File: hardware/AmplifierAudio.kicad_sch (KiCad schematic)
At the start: 50 parts, among them Q201 IRF9358, U201 MA12070P

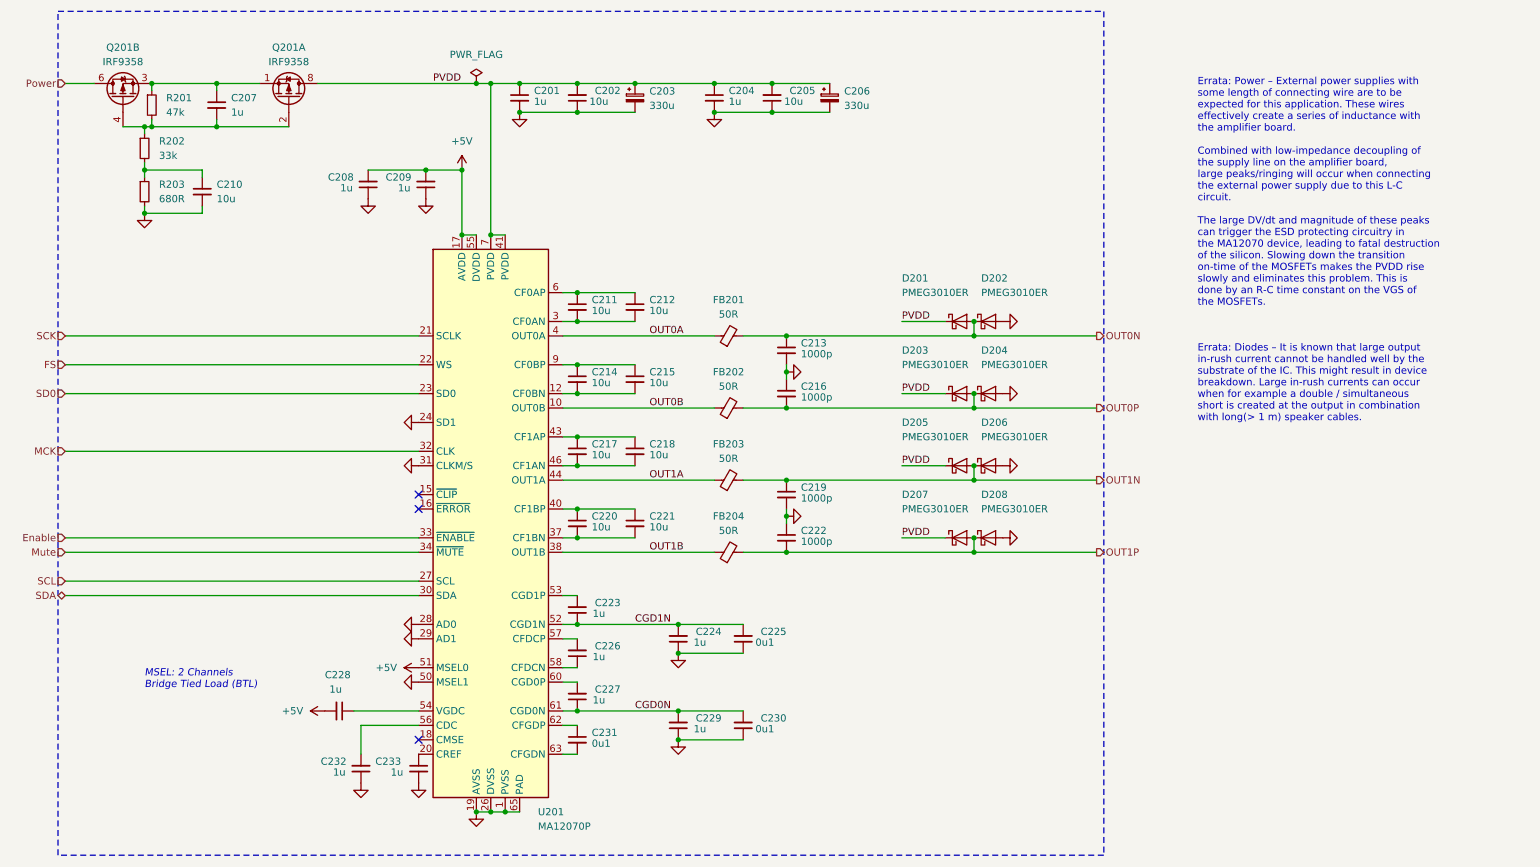
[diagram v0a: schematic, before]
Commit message: Replace Order_Number
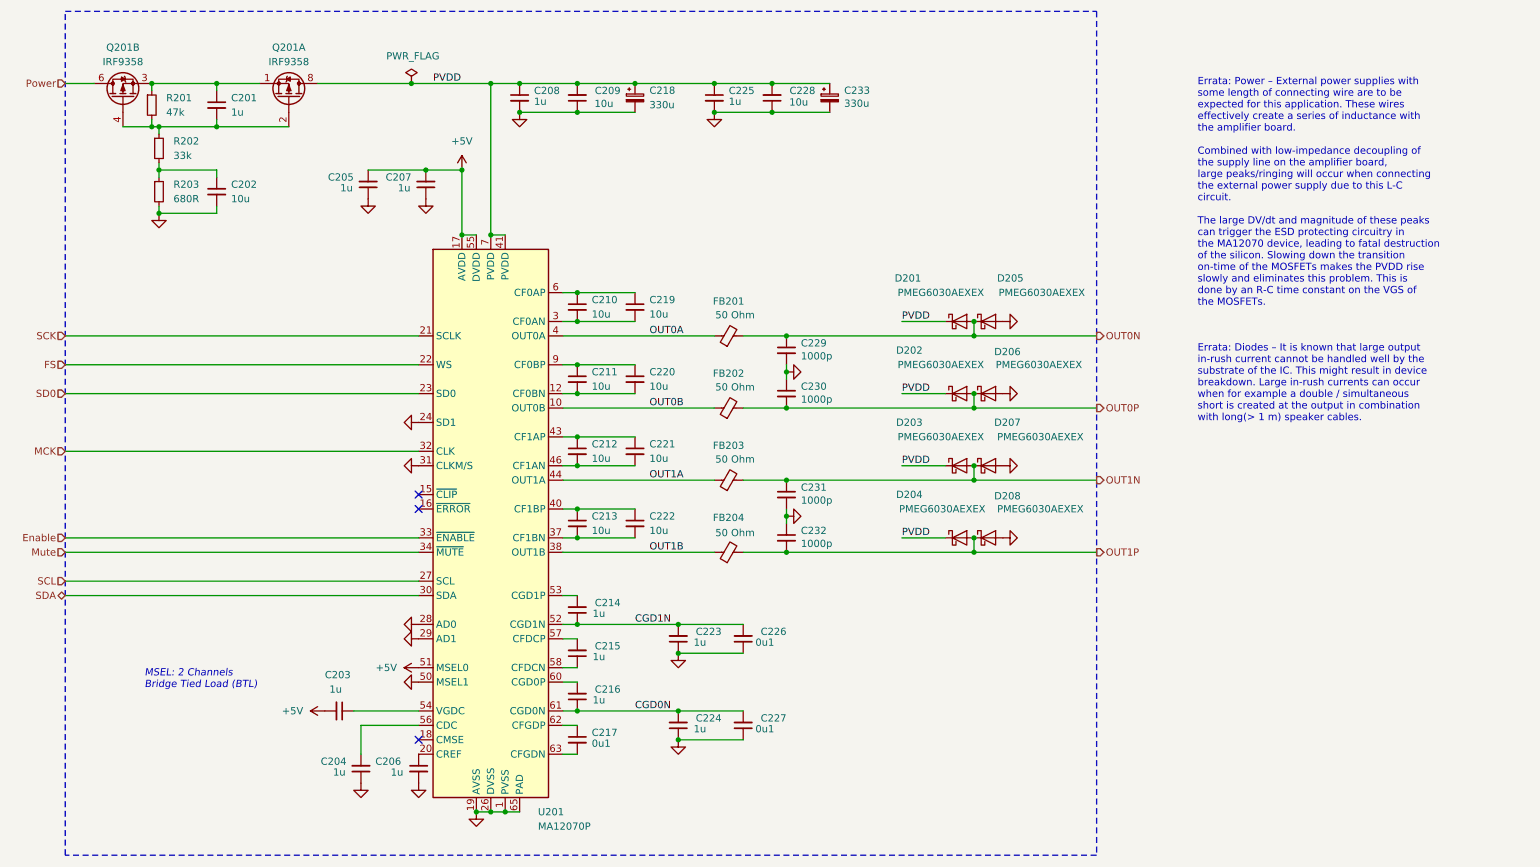
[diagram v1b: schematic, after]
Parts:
- C201: renamed from C207; footprint Capacitor_SMD:C_0603_1608Metric -> V2_Capacitor_SMD:C_0603; symbol Device:C_Small -> V2_Device:C_0603_1u; Manufacturer (none) -> TDK; Mouser (none) -> 810-CGA3E3X7R1H105K0; Product (none) -> CGA3E3X7R1H105K080AB; Rating (none) -> 50V
- C202: renamed from C210; footprint Capacitor_SMD:C_0805_2012Metric -> V2_Capacitor_SMD:C_0603; symbol Device:C_Small -> V2_Device:C_0603_10u; Manufacturer (none) -> TDK; Mouser (none) -> 810-C1608X6S1A106M; Product (none) -> C1608X6S1A106M080AC; Rating (none) -> 10V
- C203: renamed from C228; footprint Capacitor_SMD:C_0603_1608Metric -> V2_Capacitor_SMD:C_0603; symbol Device:C_Small -> V2_Device:C_0603_1u; Manufacturer (none) -> TDK; Mouser (none) -> 810-CGA3E3X7R1H105K0; Product (none) -> CGA3E3X7R1H105K080AB; Rating (none) -> 50V
- C204: renamed from C232; footprint Capacitor_SMD:C_0603_1608Metric -> V2_Capacitor_SMD:C_0603; symbol Device:C_Small -> V2_Device:C_0603_1u; Manufacturer (none) -> TDK; Mouser (none) -> 810-CGA3E3X7R1H105K0; Product (none) -> CGA3E3X7R1H105K080AB; Rating (none) -> 50V
- C205: renamed from C208; footprint Capacitor_SMD:C_0603_1608Metric -> V2_Capacitor_SMD:C_0603; symbol Device:C_Small -> V2_Device:C_0603_1u; Manufacturer (none) -> TDK; Mouser (none) -> 810-CGA3E3X7R1H105K0; Product (none) -> CGA3E3X7R1H105K080AB; Rating (none) -> 50V
- C206: renamed from C233; footprint Capacitor_SMD:C_0603_1608Metric -> V2_Capacitor_SMD:C_0603; symbol Device:C_Small -> V2_Device:C_0603_1u; Manufacturer (none) -> TDK; Mouser (none) -> 810-CGA3E3X7R1H105K0; Product (none) -> CGA3E3X7R1H105K080AB; Rating (none) -> 50V
- C207: renamed from C209; footprint Capacitor_SMD:C_0603_1608Metric -> V2_Capacitor_SMD:C_0603; symbol Device:C_Small -> V2_Device:C_0603_1u; Manufacturer (none) -> TDK; Mouser (none) -> 810-CGA3E3X7R1H105K0; Product (none) -> CGA3E3X7R1H105K080AB; Rating (none) -> 50V
- C208: renamed from C201; footprint Capacitor_SMD:C_0603_1608Metric -> V2_Capacitor_SMD:C_0603; symbol Device:C_Small -> V2_Device:C_0603_1u; Manufacturer (none) -> TDK; Mouser (none) -> 810-CGA3E3X7R1H105K0; Product (none) -> CGA3E3X7R1H105K080AB; Rating (none) -> 50V
- C209: renamed from C202; footprint Capacitor_SMD:C_0805_2012Metric -> V2_Capacitor_SMD:C_0603; symbol Device:C_Small -> V2_Device:C_0603_10u; Manufacturer (none) -> TDK; Mouser (none) -> 810-C1608X6S1A106M; Product (none) -> C1608X6S1A106M080AC; Rating (none) -> 10V
- C210: renamed from C211; footprint Capacitor_SMD:C_0805_2012Metric -> V2_Capacitor_SMD:C_0603; symbol Device:C_Small -> V2_Device:C_0603_10u; Manufacturer (none) -> TDK; Mouser (none) -> 810-C1608X6S1A106M; Product (none) -> C1608X6S1A106M080AC; Rating (none) -> 10V
- C211: renamed from C214; footprint Capacitor_SMD:C_0805_2012Metric -> V2_Capacitor_SMD:C_0603; symbol Device:C_Small -> V2_Device:C_0603_10u; Manufacturer (none) -> TDK; Mouser (none) -> 810-C1608X6S1A106M; Product (none) -> C1608X6S1A106M080AC; Rating (none) -> 10V
- C212: renamed from C217; footprint Capacitor_SMD:C_0805_2012Metric -> V2_Capacitor_SMD:C_0603; symbol Device:C_Small -> V2_Device:C_0603_10u; Manufacturer (none) -> TDK; Mouser (none) -> 810-C1608X6S1A106M; Product (none) -> C1608X6S1A106M080AC; Rating (none) -> 10V
- C213: renamed from C220; footprint Capacitor_SMD:C_0805_2012Metric -> V2_Capacitor_SMD:C_0603; symbol Device:C_Small -> V2_Device:C_0603_10u; Manufacturer (none) -> TDK; Mouser (none) -> 810-C1608X6S1A106M; Product (none) -> C1608X6S1A106M080AC; Rating (none) -> 10V
- C214: renamed from C223; footprint Capacitor_SMD:C_0603_1608Metric -> V2_Capacitor_SMD:C_0603; symbol Device:C_Small -> V2_Device:C_0603_1u; Manufacturer (none) -> TDK; Mouser (none) -> 810-CGA3E3X7R1H105K0; Product (none) -> CGA3E3X7R1H105K080AB; Rating (none) -> 50V
- C215: renamed from C226; footprint Capacitor_SMD:C_0603_1608Metric -> V2_Capacitor_SMD:C_0603; symbol Device:C_Small -> V2_Device:C_0603_1u; Manufacturer (none) -> TDK; Mouser (none) -> 810-CGA3E3X7R1H105K0; Product (none) -> CGA3E3X7R1H105K080AB; Rating (none) -> 50V
- C216: renamed from C227; footprint Capacitor_SMD:C_0603_1608Metric -> V2_Capacitor_SMD:C_0603; symbol Device:C_Small -> V2_Device:C_0603_1u; Manufacturer (none) -> TDK; Mouser (none) -> 810-CGA3E3X7R1H105K0; Product (none) -> CGA3E3X7R1H105K080AB; Rating (none) -> 50V
- C217: renamed from C231; footprint Capacitor_SMD:C_0603_1608Metric -> V2_Capacitor_SMD:C_0603; symbol Device:C_Small -> V2_Device:C_0603_0u1; Manufacturer (none) -> TDK; Mouser (none) -> 810-CGA3E2X7R1H104MA; Product (none) -> CGA3E2X7R1H104M080AA; Rating (none) -> 50V
- C218: renamed from C203; footprint Capacitor_SMD:CP_Elec_8x10 -> V2_Capacitor_SMD:CP_Elec_8x10; symbol Device:C_Polarized_Small -> V2_Device:C_Polarized_8x10.2_330u; Manufacturer (none) -> Panasonic; Mouser (none) -> 667-EEE-FT1V331GP; Product (none) -> EEE-FT1V331GP; Rating (none) -> 35V
- C219: renamed from C212; footprint Capacitor_SMD:C_0805_2012Metric -> V2_Capacitor_SMD:C_0603; symbol Device:C_Small -> V2_Device:C_0603_10u; Manufacturer (none) -> TDK; Mouser (none) -> 810-C1608X6S1A106M; Product (none) -> C1608X6S1A106M080AC; Rating (none) -> 10V
- C220: renamed from C215; footprint Capacitor_SMD:C_0805_2012Metric -> V2_Capacitor_SMD:C_0603; symbol Device:C_Small -> V2_Device:C_0603_10u; Manufacturer (none) -> TDK; Mouser (none) -> 810-C1608X6S1A106M; Product (none) -> C1608X6S1A106M080AC; Rating (none) -> 10V
- C221: renamed from C218; footprint Capacitor_SMD:C_0805_2012Metric -> V2_Capacitor_SMD:C_0603; symbol Device:C_Small -> V2_Device:C_0603_10u; Manufacturer (none) -> TDK; Mouser (none) -> 810-C1608X6S1A106M; Product (none) -> C1608X6S1A106M080AC; Rating (none) -> 10V
- C222: renamed from C221; footprint Capacitor_SMD:C_0805_2012Metric -> V2_Capacitor_SMD:C_0603; symbol Device:C_Small -> V2_Device:C_0603_10u; Manufacturer (none) -> TDK; Mouser (none) -> 810-C1608X6S1A106M; Product (none) -> C1608X6S1A106M080AC; Rating (none) -> 10V
- C223: renamed from C224; footprint Capacitor_SMD:C_0603_1608Metric -> V2_Capacitor_SMD:C_0603; symbol Device:C_Small -> V2_Device:C_0603_1u; Manufacturer (none) -> TDK; Mouser (none) -> 810-CGA3E3X7R1H105K0; Product (none) -> CGA3E3X7R1H105K080AB; Rating (none) -> 50V
- C224: renamed from C229; footprint Capacitor_SMD:C_0603_1608Metric -> V2_Capacitor_SMD:C_0603; symbol Device:C_Small -> V2_Device:C_0603_1u; Manufacturer (none) -> TDK; Mouser (none) -> 810-CGA3E3X7R1H105K0; Product (none) -> CGA3E3X7R1H105K080AB; Rating (none) -> 50V
- C225: renamed from C204; footprint Capacitor_SMD:C_0603_1608Metric -> V2_Capacitor_SMD:C_0603; symbol Device:C_Small -> V2_Device:C_0603_1u; Manufacturer (none) -> TDK; Mouser (none) -> 810-CGA3E3X7R1H105K0; Product (none) -> CGA3E3X7R1H105K080AB; Rating (none) -> 50V
- C226: renamed from C225; footprint Capacitor_SMD:C_0603_1608Metric -> V2_Capacitor_SMD:C_0603; symbol Device:C_Small -> V2_Device:C_0603_0u1; Manufacturer (none) -> TDK; Mouser (none) -> 810-CGA3E2X7R1H104MA; Product (none) -> CGA3E2X7R1H104M080AA; Rating (none) -> 50V
- C227: renamed from C230; footprint Capacitor_SMD:C_0603_1608Metric -> V2_Capacitor_SMD:C_0603; symbol Device:C_Small -> V2_Device:C_0603_0u1; Manufacturer (none) -> TDK; Mouser (none) -> 810-CGA3E2X7R1H104MA; Product (none) -> CGA3E2X7R1H104M080AA; Rating (none) -> 50V
- C228: renamed from C205; footprint Capacitor_SMD:C_0805_2012Metric -> V2_Capacitor_SMD:C_0603; symbol Device:C_Small -> V2_Device:C_0603_10u; Manufacturer (none) -> TDK; Mouser (none) -> 810-C1608X6S1A106M; Product (none) -> C1608X6S1A106M080AC; Rating (none) -> 10V
- C229: renamed from C213; footprint Capacitor_SMD:C_0603_1608Metric -> V2_Capacitor_SMD:C_0603; symbol Device:C_Small -> V2_Device:C_0603_1000p; Manufacturer (none) -> TDK; Mouser (none) -> 810-C1608C0G1H102J; Product (none) -> C1608C0G1H102J080AA; Rating (none) -> 50V
- C230: renamed from C216; footprint Capacitor_SMD:C_0603_1608Metric -> V2_Capacitor_SMD:C_0603; symbol Device:C_Small -> V2_Device:C_0603_1000p; Manufacturer (none) -> TDK; Mouser (none) -> 810-C1608C0G1H102J; Product (none) -> C1608C0G1H102J080AA; Rating (none) -> 50V
- C231: renamed from C219; footprint Capacitor_SMD:C_0603_1608Metric -> V2_Capacitor_SMD:C_0603; symbol Device:C_Small -> V2_Device:C_0603_1000p; Manufacturer (none) -> TDK; Mouser (none) -> 810-C1608C0G1H102J; Product (none) -> C1608C0G1H102J080AA; Rating (none) -> 50V
- C232: renamed from C222; footprint Capacitor_SMD:C_0603_1608Metric -> V2_Capacitor_SMD:C_0603; symbol Device:C_Small -> V2_Device:C_0603_1000p; Manufacturer (none) -> TDK; Mouser (none) -> 810-C1608C0G1H102J; Product (none) -> C1608C0G1H102J080AA; Rating (none) -> 50V
- C233: renamed from C206; footprint Capacitor_SMD:CP_Elec_8x10 -> V2_Capacitor_SMD:CP_Elec_8x10; symbol Device:C_Polarized_Small -> V2_Device:C_Polarized_8x10.2_330u; Manufacturer (none) -> Panasonic; Mouser (none) -> 667-EEE-FT1V331GP; Product (none) -> EEE-FT1V331GP; Rating (none) -> 35V
- D201, D208: value PMEG3010ER -> PMEG6030AEXEX; footprint Diode_SMD:Nexperia_CFP3_SOD-123W -> V2_Diode_SMD:D_SOD-123HP; symbol V2_Diode:PMEG3010ER -> V2_Diode:PMEG6030AEXEX; Manufacturer (none) -> Nexperia; Mouser (none) -> 771-PMEG6030AEXEX; Product (none) -> PMEG6030AEXEX
- D202: renamed from D203; value PMEG3010ER -> PMEG6030AEXEX; footprint Diode_SMD:Nexperia_CFP3_SOD-123W -> V2_Diode_SMD:D_SOD-123HP; symbol V2_Diode:PMEG3010ER -> V2_Diode:PMEG6030AEXEX; Manufacturer (none) -> Nexperia; Mouser (none) -> 771-PMEG6030AEXEX; Product (none) -> PMEG6030AEXEX
- D203: renamed from D205; value PMEG3010ER -> PMEG6030AEXEX; footprint Diode_SMD:Nexperia_CFP3_SOD-123W -> V2_Diode_SMD:D_SOD-123HP; symbol V2_Diode:PMEG3010ER -> V2_Diode:PMEG6030AEXEX; Manufacturer (none) -> Nexperia; Mouser (none) -> 771-PMEG6030AEXEX; Product (none) -> PMEG6030AEXEX
- D204: renamed from D207; value PMEG3010ER -> PMEG6030AEXEX; footprint Diode_SMD:Nexperia_CFP3_SOD-123W -> V2_Diode_SMD:D_SOD-123HP; symbol V2_Diode:PMEG3010ER -> V2_Diode:PMEG6030AEXEX; Manufacturer (none) -> Nexperia; Mouser (none) -> 771-PMEG6030AEXEX; Product (none) -> PMEG6030AEXEX
- D205: renamed from D202; value PMEG3010ER -> PMEG6030AEXEX; footprint Diode_SMD:Nexperia_CFP3_SOD-123W -> V2_Diode_SMD:D_SOD-123HP; symbol V2_Diode:PMEG3010ER -> V2_Diode:PMEG6030AEXEX; Manufacturer (none) -> Nexperia; Mouser (none) -> 771-PMEG6030AEXEX; Product (none) -> PMEG6030AEXEX
- D206: renamed from D204; value PMEG3010ER -> PMEG6030AEXEX; footprint Diode_SMD:Nexperia_CFP3_SOD-123W -> V2_Diode_SMD:D_SOD-123HP; symbol V2_Diode:PMEG3010ER -> V2_Diode:PMEG6030AEXEX; Manufacturer (none) -> Nexperia; Mouser (none) -> 771-PMEG6030AEXEX; Product (none) -> PMEG6030AEXEX
- D207: renamed from D206; value PMEG3010ER -> PMEG6030AEXEX; footprint Diode_SMD:Nexperia_CFP3_SOD-123W -> V2_Diode_SMD:D_SOD-123HP; symbol V2_Diode:PMEG3010ER -> V2_Diode:PMEG6030AEXEX; Manufacturer (none) -> Nexperia; Mouser (none) -> 771-PMEG6030AEXEX; Product (none) -> PMEG6030AEXEX
- FB201, FB202, FB203, FB204: value 50R -> 50 Ohm; footprint Inductor_SMD:L_1206_3216Metric -> V2_Inductor_SMD:L_1206; symbol Device:FerriteBead_Small -> V2_Device:FerriteBead_1206_50Ohm; Manufacturer (none) -> Fair-Rite; Mouser (none) -> 623-2512065007Y6; Product (none) -> 2512065007Y6
- Q201: footprint Package_SO:SOIC-8_3.9x4.9mm_P1.27mm -> V2_Package_SO:SOIC-8_3.9x4.9mm_P1.27mm; Manufacturer (none) -> Infineon Technologies; Mouser (none) -> 942-IRF9358TRPBF; Polarity (none) -> P; Product (none) -> IRF9358TRPBF; Rating (none) -> 30V
- R201: footprint Resistor_SMD:R_0603_1608Metric -> V2_Resistor_SMD:R_0603; symbol Device:R_Small -> V2_Device:R_0603_47k; Manufacturer (none) -> Vishay; Mouser (none) -> 71-RCS060347K0FKEA; Product (none) -> RCS060347K0FKEA; Rating (none) -> 250mW
- R202: footprint Resistor_SMD:R_0603_1608Metric -> V2_Resistor_SMD:R_0603; symbol Device:R_Small -> V2_Device:R_0603_33k; Manufacturer (none) -> Vishay; Mouser (none) -> 71- 71-CRCW060333K0FKEAH; Product (none) -> CRCW060333K0FKEAHP; Rating (none) -> 330mW
- R203: footprint Resistor_SMD:R_0603_1608Metric -> V2_Resistor_SMD:R_0603; symbol Device:R_Small -> V2_Device:R_0603_680R; Manufacturer (none) -> Vishay; Mouser (none) -> 71-RCS0603680RFKEA; Product (none) -> RCS0603680RFKEA; Rating (none) -> 250mW
- U201: Manufacturer (none) -> Infineon Technologies; Mouser (none) -> 726-MA12070PXUMA1; Product (none) -> MA12070PXUMA1
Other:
- moved on the sheet: C202, R202, R203

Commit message: Update Library
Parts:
- C201, C203, C204, C205, C206, C207, C208, C214, C215, C216, C223, C224, C225: symbol V2_Device:C_0603_1u -> V2_Capacitor:0603_1u
- C202, C209, C210, C211, C212, C213, C219, C220, C221, C222, C228: symbol V2_Device:C_0603_10u -> V2_Capacitor:0603_10u
- C217, C226, C227: symbol V2_Device:C_0603_0u1 -> V2_Capacitor:0603_0u1
- C218, C233: symbol V2_Device:C_Polarized_8x10.2_330u -> V2_Capacitor:Polarized_8x10.2_330u
- C229, C230, C231, C232: symbol V2_Device:C_0603_1000p -> V2_Capacitor:0603_1000p
- FB201, FB202, FB203, FB204: value 50 Ohm -> ~; symbol V2_Device:FerriteBead_1206_50Ohm -> V2_Inductor:FerriteBead_1206_50Ohm
- R201: symbol V2_Device:R_0603_47k -> V2_Resistor:0603_47k
- R202: symbol V2_Device:R_0603_33k -> V2_Resistor:0603_33k
- R203: symbol V2_Device:R_0603_680R -> V2_Resistor:0603_680R

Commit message: Update
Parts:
- FB201, FB202, FB203, FB204: value ~ -> 50 Ω
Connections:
- net Source: now reaches C201.1, Q201.1 (S1), Q201.3 (S2), R201.1
- net Gate: now reaches C201.2, Q201.2 (G1), Q201.4 (G2), R201.2, R202.1
- net PVDD renamed +PVDD
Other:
- moved on the sheet: C202, R202, R203
